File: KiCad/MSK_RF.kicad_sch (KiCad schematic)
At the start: 59 parts, among them J1 Conn_ARM_JTAG_SWD_10, J5 USB_B_Micro, U1 STM32WLE5CCU6, U3 TLV70233_SOT23-5, Y1 32.768 kHz, Y2 32MHz

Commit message: Second button
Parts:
- added C?: 100 nF, symbol pspice:CAP
- added D?: PESD5V0L4UW, Package_TO_SOT_SMD:SOT-665, symbol Power_Protection:PESD5V0L4UW
- added R?: 1k, symbol Device:R
- added SW?: SW_Push, symbol Switch:SW_Push
- C11, C9: value (none) -> 4.7pF
- C14: value (none) -> 5.1pF
- C15: value (none) -> 22pF
- C?: value (none) -> 1nF
- C?: value (none) -> 10pF
- C?: value (none) -> 0.1uF
- D?: value (none) -> PESD5V0L4UW; footprint (none) -> Package_TO_SOT_SMD:SOT-665
- J2, J3: value (none) -> Conn_01x12; footprint (none) -> Connector_PinSocket_1.27mm:PinSocket_1x12_P1.27mm_Vertical
- J?: value (none) -> Conn_Coaxial
- JP?: value (none) -> Jumper_2_Open
- JP?: value (none) -> Jumper_2_Bridged
- L2: value (none) -> 39nH
- L4: value (none) -> 56n
- L5: value (none) -> 5.6nH
- L6: value (none) -> 16nH
- R?: value (none) -> 10k
- R?: value (none) -> 1k
- R?: value (none) -> 100R
- SW?: value (none) -> SW_Push
- U?: value (none) -> ADG918BRM; footprint (none) -> Package_SO:MSOP-8_3x3mm_P0.65mm
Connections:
- net GND: now also C?.1
- net PA1: now also R?.1
- new net: D?.1 (K1), R?.2, SW?.1
- new net: C?.2, D?.2 (A), SW?.2
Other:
- note added: "RESET BUTTON"
- note added: "USER BUTTON 2"
- moved on the sheet: C1, C17, C18, C19, C2, C20, C21, C22, C23, C27, C28, C29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

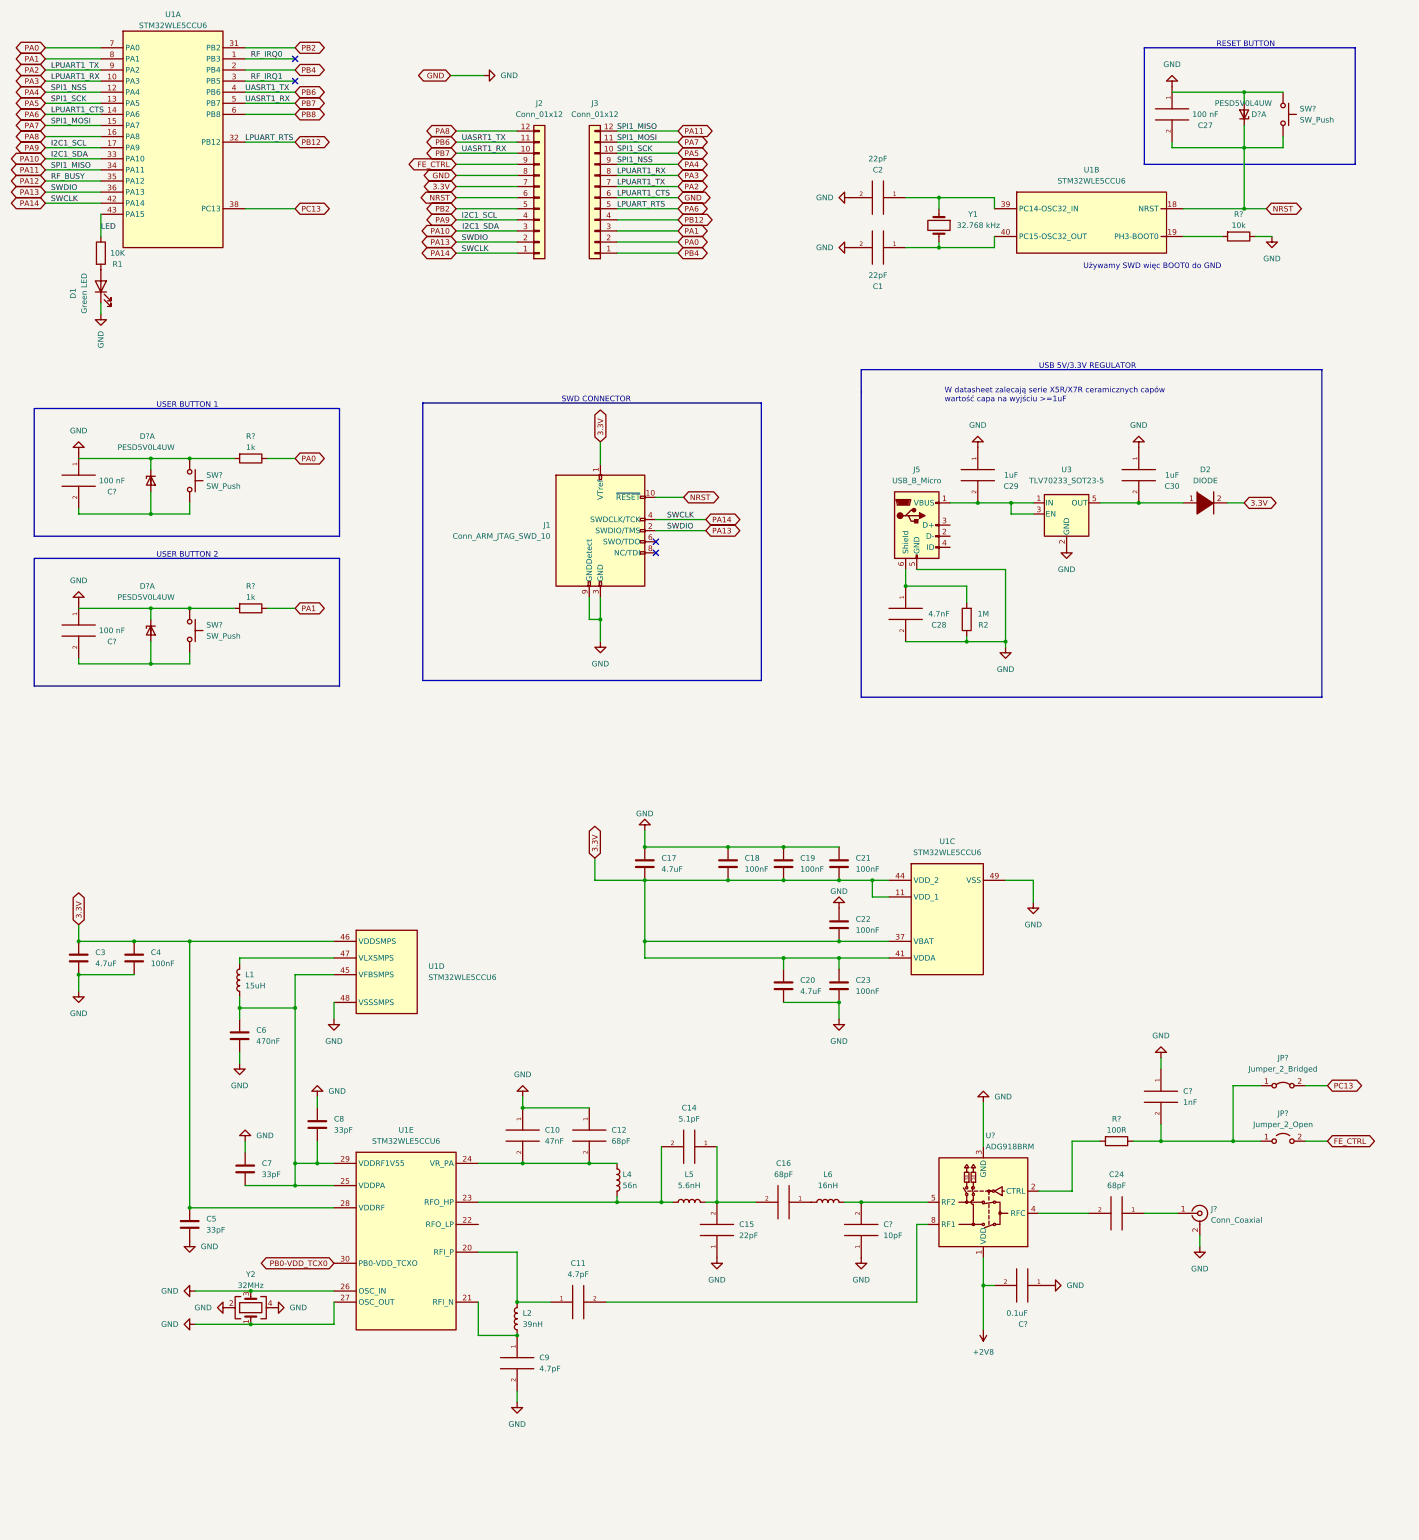
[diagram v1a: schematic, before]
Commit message: added connectors footprint
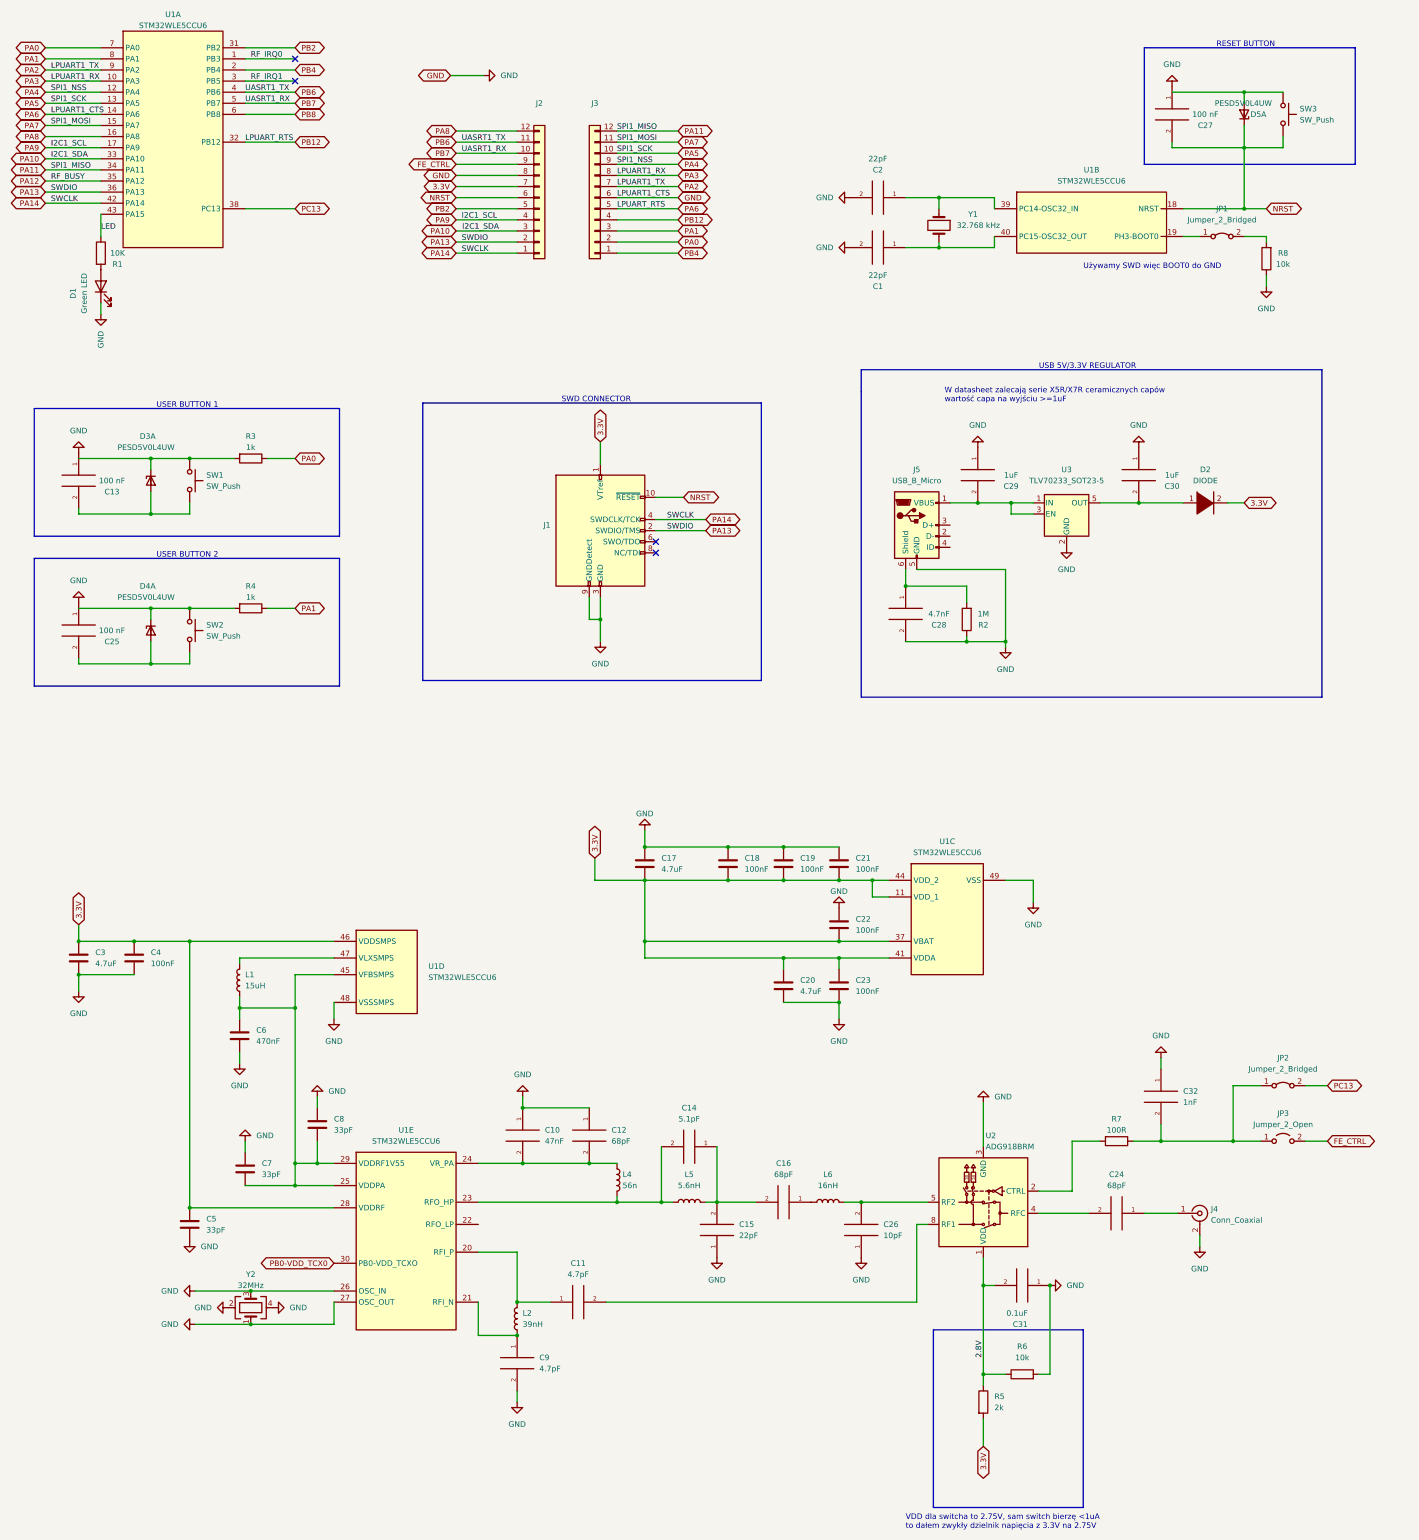
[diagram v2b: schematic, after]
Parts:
- added JP1: Jumper_2_Bridged, symbol Jumper:Jumper_2_Bridged
- added R5: 2k, symbol Device:R
- added R6: 10k, symbol Device:R
- J1: value Conn_ARM_JTAG_SWD_10 -> (none)
- J2, J3: value Conn_01x12 -> (none); footprint Connector_PinSocket_1.27mm:PinSocket_1x12_P1.27mm_Vertical -> (none)
- gave numbers to parts that had none: 19
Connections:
- net 3.3V: now also R5.2
- net GND: now also R6.2
- net at U1.19 (PH3-BOOT0): now also JP1.1 (A); no longer R8.2
- net +2V8 renamed 2.8V
- net 2.8V: now also R5.1, R6.1
- new net: JP1.2 (B), R8.2
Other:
- note added: "VDD dla switcha to 2.75V, sam switch bierzę <1uA to dałem zwykły dzielnik napięcia z 3.3V na 2.75V"
- moved on the sheet: R8
